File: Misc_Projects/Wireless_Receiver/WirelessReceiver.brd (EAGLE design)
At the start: 27.7 x 66 mm, 10 parts, among them Q1 600mA/40V, Q2 600mA/40V, Q3 600mA/40V, X2 JST-XH-06-PIN-LONG-PAD

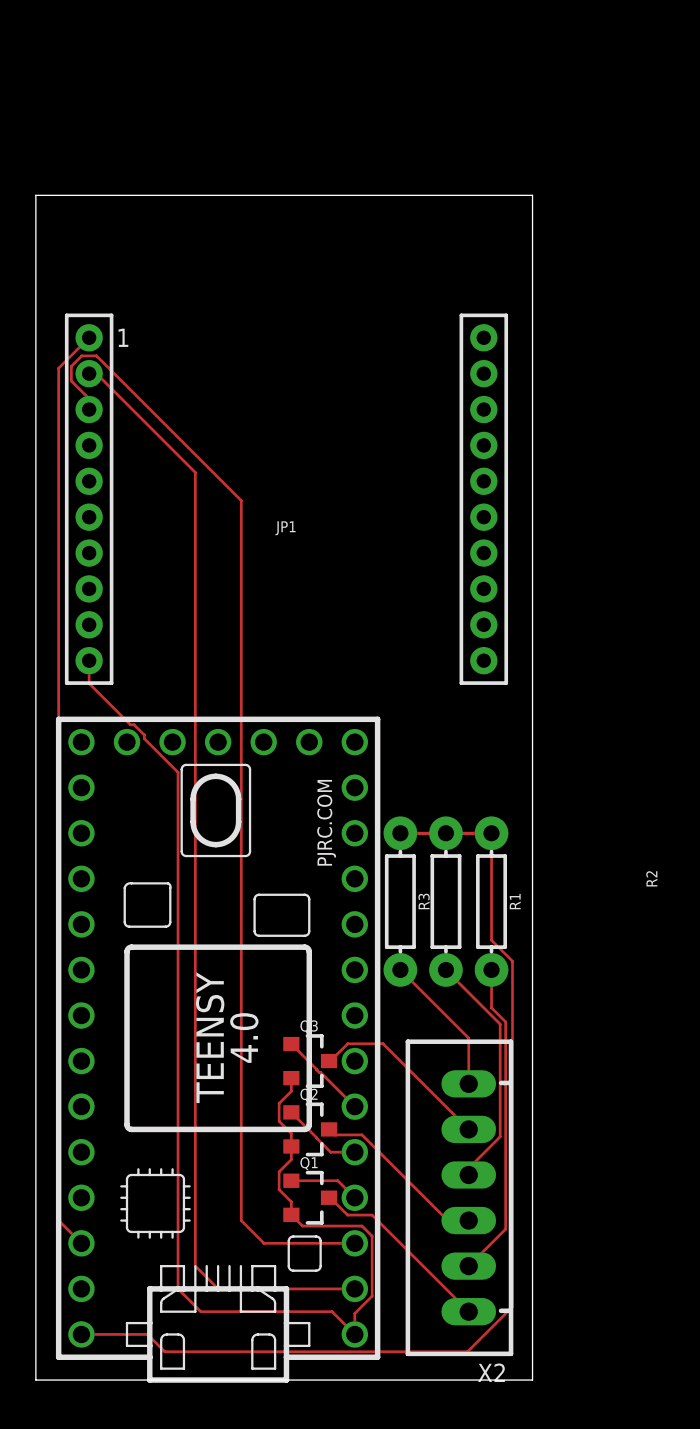
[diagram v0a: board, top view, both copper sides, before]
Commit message: Changed Wireless Receiver Xbee 3 Pro to Xbee Pro S3B
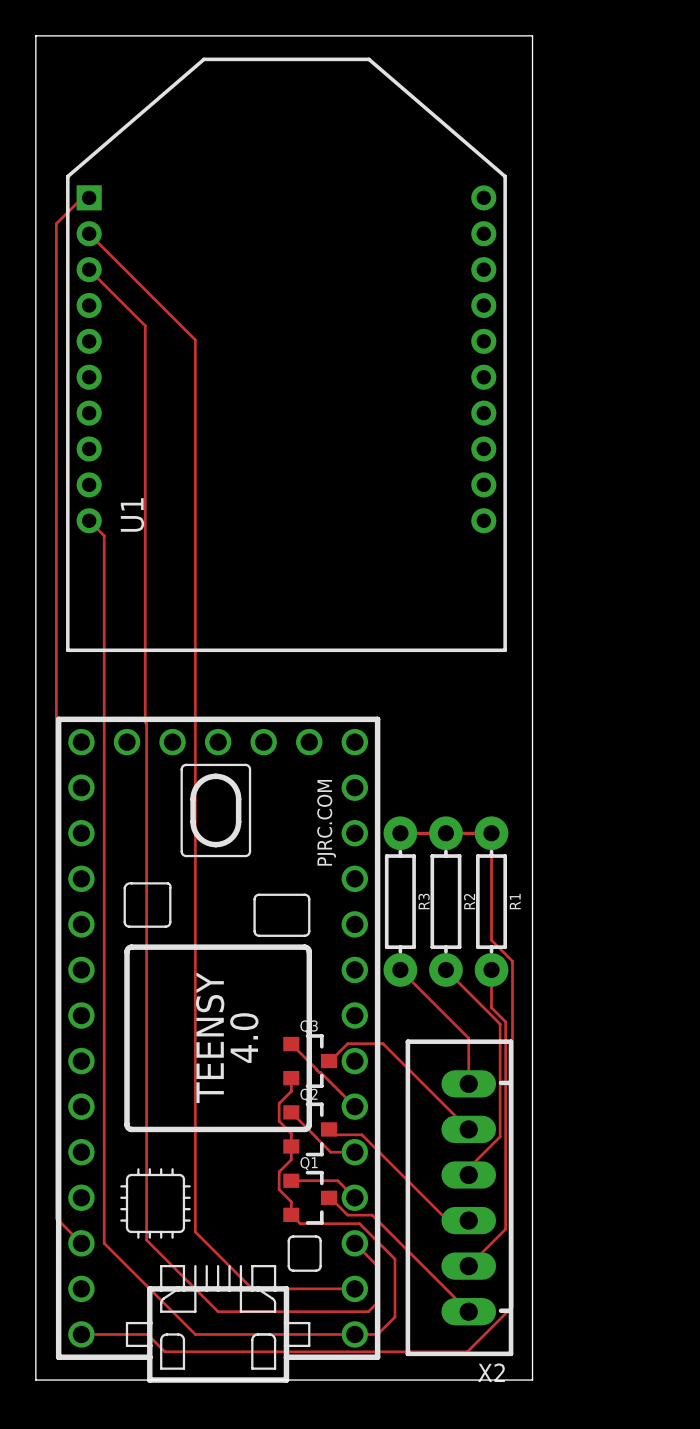
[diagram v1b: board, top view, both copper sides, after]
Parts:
- removed JP1: (no value), SparkFun-RF:XBEE
- added U1: XBEE_PRO_S3B, GTOR - Microcontroller:XBEE_PRO_S3B
- moved FRAME1 8.98 mm to (-20.3, 67.3)
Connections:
- removed net N$1: JP1.2, U$1.0/RX
- removed net N$2: JP1.3, U$1.1/TX
- new net RX1: U$1.0/RX, U1.2
- new net TX1: U$1.1/TX, U1.3
- net 3V3: now also U1.1; no longer JP1.1
- net GND: now also U1.10; no longer JP1.10
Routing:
- net TX1: track 0.00 -> 74.0 mm
- net RX1: track 0.00 -> 68.3 mm
- net N$2: track 62.9 -> 0.00 mm
- net N$1: track 61.9 -> 0.00 mm
- net GND: track 67.7 -> 78.1 mm
- net 3V3: track 51.7 -> 59.8 mm
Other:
- board size 27.7 x 66 mm -> 27.7 x 74.9 mm
